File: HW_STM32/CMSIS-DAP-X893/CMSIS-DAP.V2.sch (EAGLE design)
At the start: 35 parts, among them IC1 STM32F103CBT6, J3 USB-4-A-SMD, Q1 8M, U7 TPS73033, X1 USB-SMD

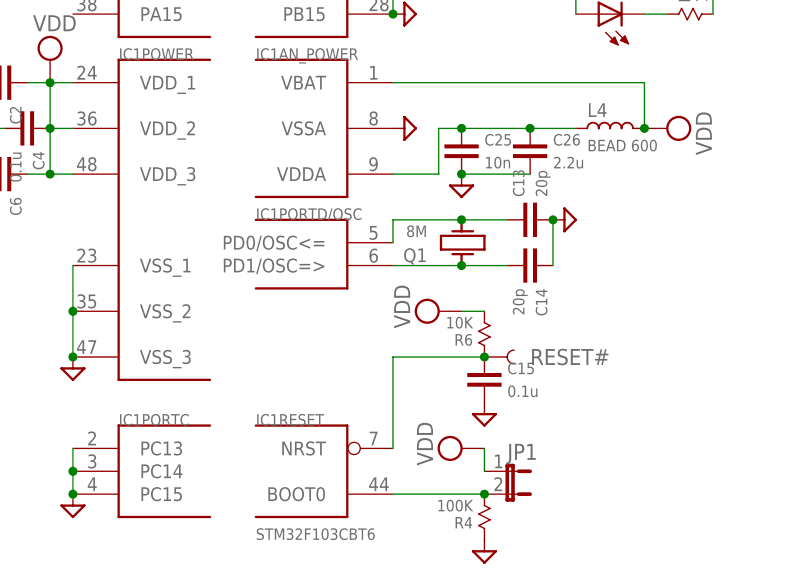
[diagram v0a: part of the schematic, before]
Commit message: Fix RESET pin
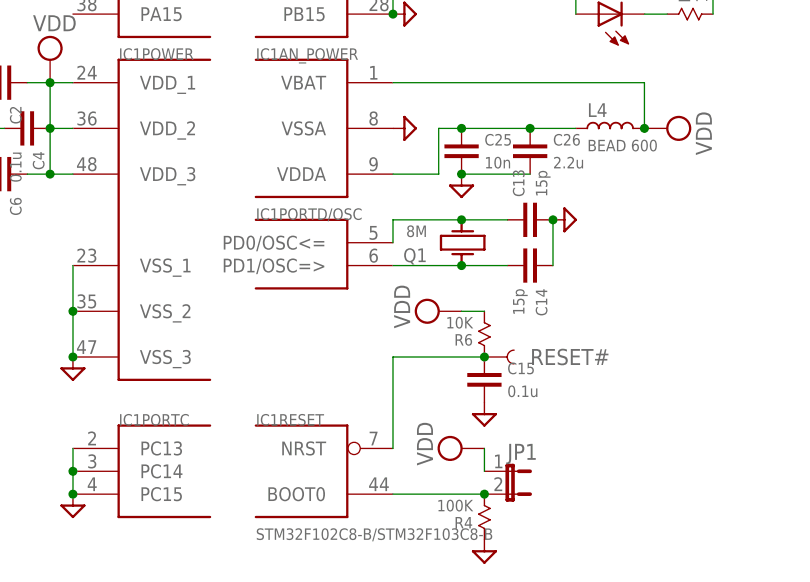
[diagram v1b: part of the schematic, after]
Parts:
- C13, C14: value 20p -> 15p
- IC1: value STM32F103CBT6 -> STM32F102C8-B/STM32F103C8-B
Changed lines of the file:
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@@
 <part name="C6" library="X893" deviceset="CAP" device="-0603" value="0.1u"/>
 <part name="Q1" library="X893" deviceset="CRYSTAL" device="-KX-9A" value="8M"/>
-<part name="C13" library="X893" deviceset="CAP" device="-0603" value="20p"/>
-<part name="C14" library="X893" deviceset="CAP" device="-0603" value="20p"/>
+<part name="C13" library="X893" deviceset="CAP" device="-0603" value="15p"/>
+<part name="C14" library="X893" deviceset="CAP" device="-0603" value="15p"/>
 <part name="SUPPLY9" library="supply2" deviceset="GND" device=""/>
 <part name="R4" library="X893" deviceset="RESISTOR" device="-0603" value="100K"/>
@@
 <part name="C29" library="X893" deviceset="CAP" device="-0603" value="4.7u"/>
 <part name="SUPPLY1" library="supply2" deviceset="VEE" device=""/>
-<part name="IC1" library="stm32" deviceset="STM32F10XCXT6" device="" value="STM32F103CBT6"/>
+<part name="IC1" library="stm32" deviceset="STM32F10XCXT6" device="" value="STM32F102C8-B/STM32F103C8-B"/>
 <part name="SUPPLY3" library="supply2" deviceset="GND" device=""/>
 <part name="SUPPLY4" library="supply2" deviceset="GND" device=""/>

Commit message: Add HEX file
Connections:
- net PA10 renamed PA10-RX
- net PA9 renamed PA9-TX
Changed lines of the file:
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@@
 <?xml version="1.0" encoding="utf-8"?>
 <!DOCTYPE eagle SYSTEM "eagle.dtd">
-<eagle version="6.4">
+<eagle version="7.1.0">
 <drawing>
 <settings>
@@
 </segment>
 </net>
-<net name="PA9" class="0">
+<net name="PA9-TX" class="0">
 <segment>
 <wire x1="218.44" y1="134.62" x2="193.04" y2="134.62" width="0.1524" layer="91"/>
@@
 </segment>
 </net>
-<net name="PA10" class="0">
+<net name="PA10-RX" class="0">
 <segment>
 <wire x1="218.44" y1="132.08" x2="190.5" y2="132.08" width="0.1524" layer="91"/>
